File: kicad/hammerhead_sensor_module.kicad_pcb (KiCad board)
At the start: 6 copper layers, 87.5 x 58.8 mm, 138 parts, among them IC1 RT6254BHGJ6F, IC3 RT6254BHGJ6F, IC4 MAX98357AETE+T, IC6 TXB0108RGYR, J1 COMMS CONN, J10 12402012E212A, J2 APCI0105-P001A, J3 SMN-303, J4 Conn_01x22_Female, J5 Conn_01x22_Female, J6 Conn_01x03, J7 SM04B-SRSS-TBLFSN, J8 SM04B-SRSS-TBLFSN, J9 B6B-XH-A, SW1 218-2LPSTRF, U1 TPD4E05U06DQAR, U10 TPD4E05U06DQAR, U11 TPD4E05U06DQAR, U12 467651001, U13 RT9742SNGV, U14 TPD4E05U06DQAR, U15 TPD4E05U06DQAR, U16 TPD4E05U06DQAR, U17 TPD4E05U06DQAR, U18 TPD4E05U06DQAR, U19 TPD4E05U06DQAR, U2 MMBT3904TT1G, U3 TLV75733PDBVR, U4 TPD4E05U06DQAR, U5 TPD4E05U06DQAR, U6 TPD4E05U06DQAR, U7 TPD4E05U06DQAR, U8 TPD4E05U06DQAR, U9 TPD4E05U06DQAR

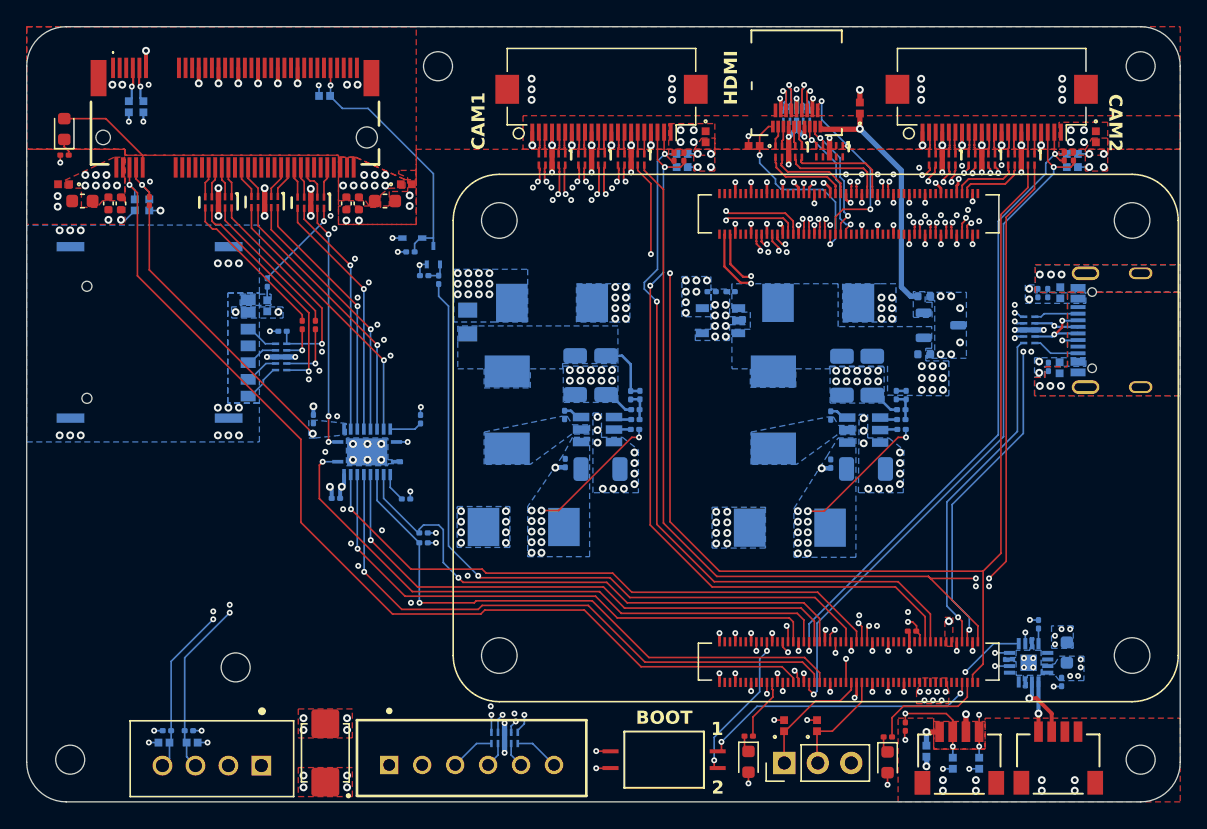
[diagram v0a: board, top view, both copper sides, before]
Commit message: update changelog v0.0.0->v0.0.1
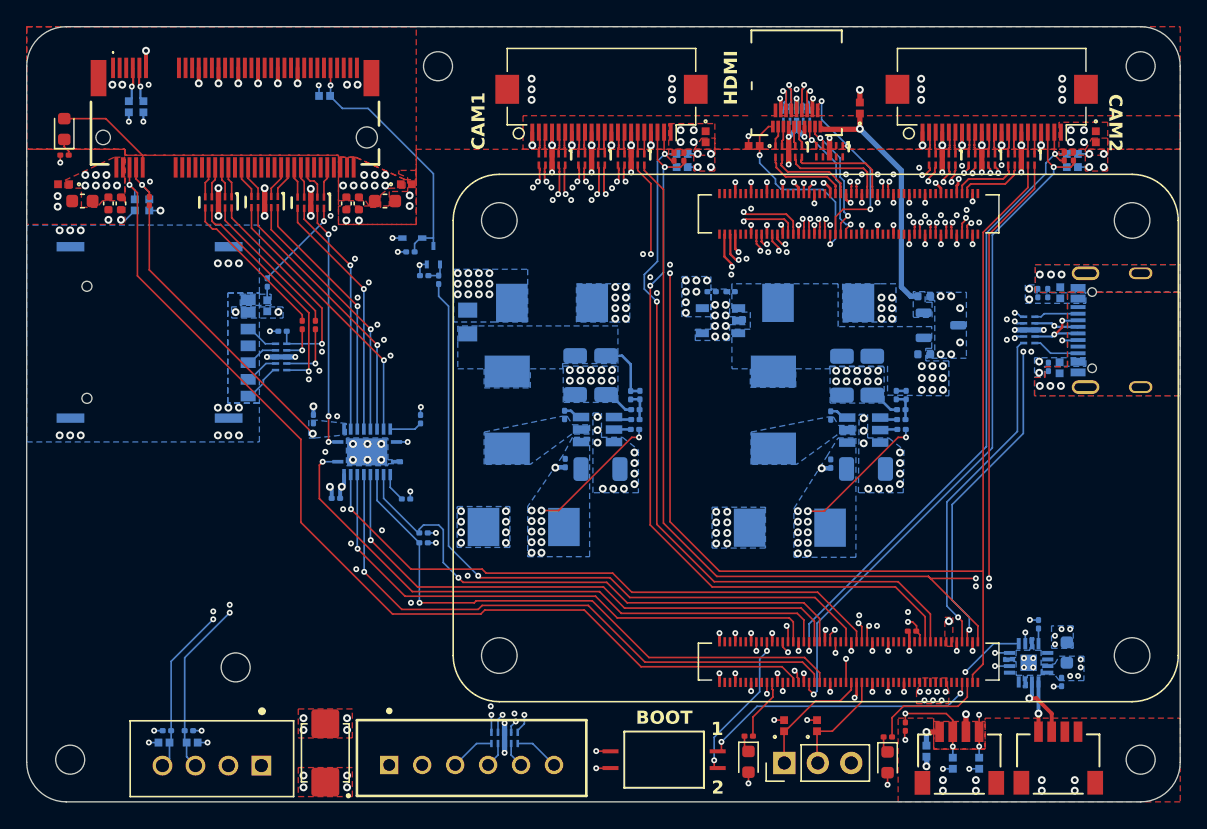
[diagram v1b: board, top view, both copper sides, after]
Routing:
- net GND: track 132.2 -> 132.7 mm, vias 347 -> 355

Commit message: add docs and cleanup
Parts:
- added R26: 2.2k 1%, Resistor_SMD:R_0201_0603Metric, B.Cu at (86.3, 52.9)
- added R30: 2.2k 1%, Resistor_SMD:R_0201_0603Metric, B.Cu at (86.3, 52.1)
- added R32: 22 <1%, Resistor_SMD:R_0201_0603Metric, B.Cu at (78.2, 54.2)
- moved R29 2.09 mm to (60.5, 35.4)
- moved D2 1.80 mm to (60.5, 37.3), turned to -90 degrees
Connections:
- D2 pad 2: /SIM7600G-H-M2B/LED1 -> 4V
- Module1 pad 91: unconnected-(Module1A-BT_nDisable-Pad91) -> GND
- R14 pad 1: 1.8V -> 3.3V
- R29 pad 1: GND -> Net-(D2-K)
- R29 pad 2: Net-(D2-K) -> /SIM7600G-H-M2B/LED1
- U17 pad 10: /SIM7600G-H-M2B/USIM_CLK -> Net-(R32-Pad1)
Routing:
- net 1.8V: track 88.6 -> 73.0 mm, vias 3 -> 4
- net 3.3V: track 20.5 -> 29.9 mm, vias 26 -> 27
- net GND: track 132.7 -> 134.6 mm, vias 355 -> 354
- net /SIM7600G-H-M2B/I2C_SDA: track 20.6 -> 22.3 mm
- net /SIM7600G-H-M2B/I2C_SCL: track 21.0 -> 22.3 mm
- net Net-(R32-Pad1): track 0.00 -> 0.85 mm
- net /SIM7600G-H-M2B/LED1: track 8.01 -> 7.46 mm

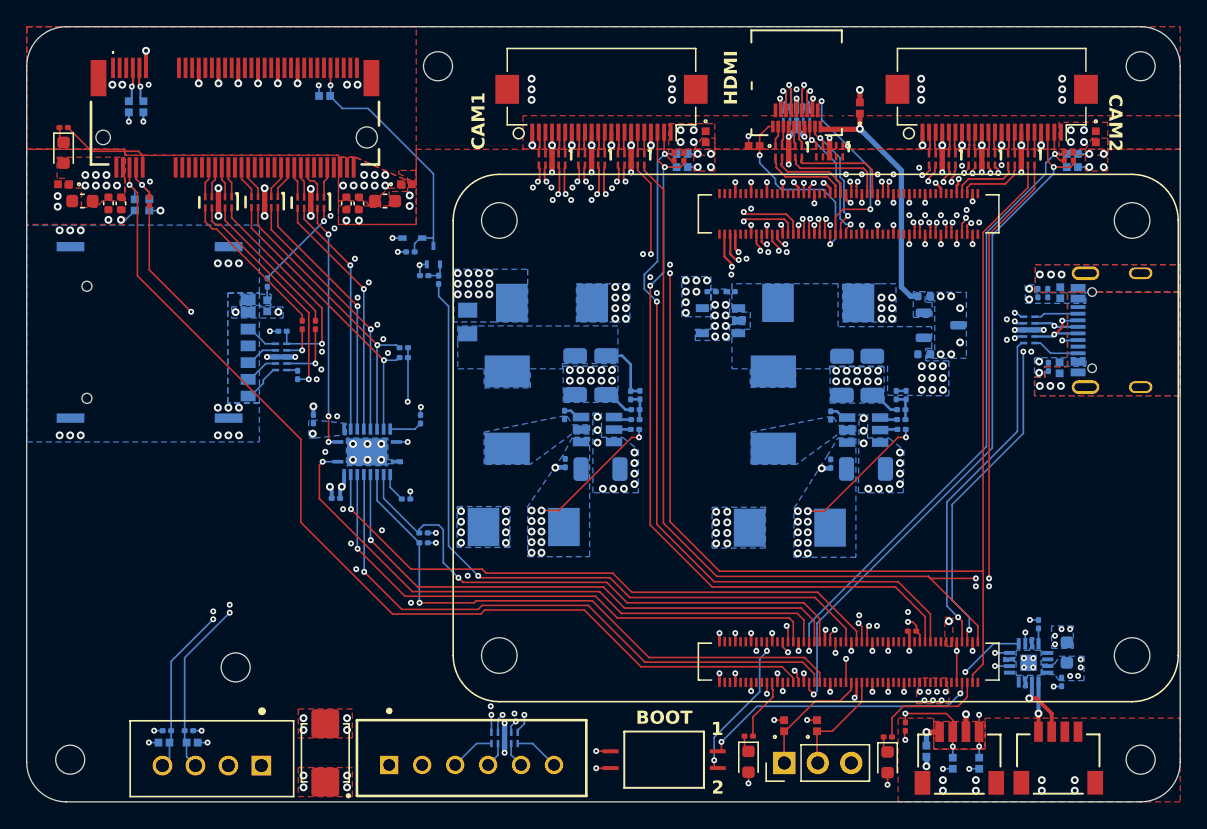
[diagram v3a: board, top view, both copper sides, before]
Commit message: assign 3d models
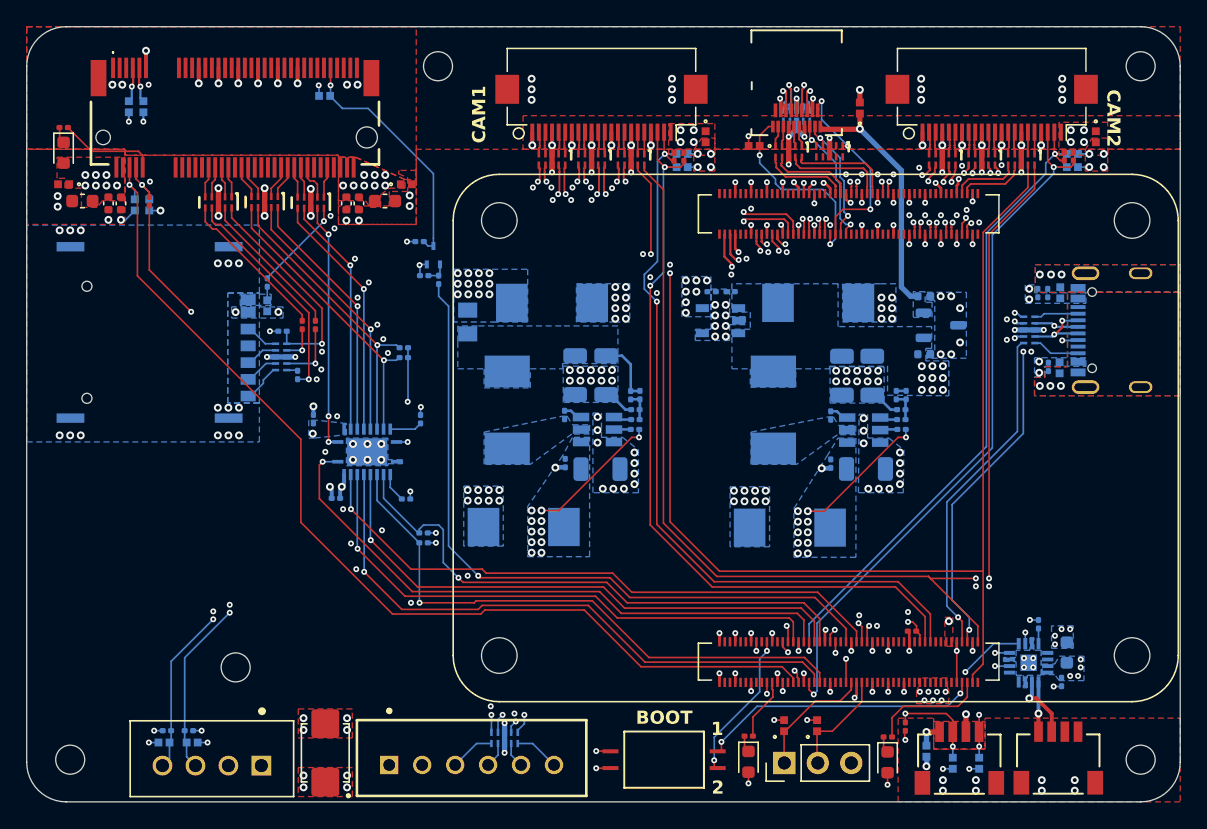
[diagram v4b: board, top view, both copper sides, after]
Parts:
- removed the D1 at (86.9, 43.8)
- moved C27 1.05 mm to (87.5, 44.0)
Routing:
- net /SIM7600G-H-M2B/RESET: track 20.1 -> 18.8 mm
- net GND: track 134.6 -> 133.8 mm, vias 354 -> 353
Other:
- board text removed: "HDMI"

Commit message: add power testpoints, add debug gpio testpoints, add comms testpoints, add logo, add component orientation silkscreen, add board name and revision silkscreen
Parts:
- added TP1: TestPoint, TestPoint:TestPoint_Pad_1.0x1.0mm, B.Cu at (134.6, 70.8)
- added TP10: TestPoint, TestPoint:TestPoint_Pad_1.0x1.0mm, B.Cu at (77.8, 36.0)
- added TP11: TestPoint, TestPoint:TestPoint_Pad_1.0x1.0mm, B.Cu at (103.0, 65.8)
- added TP12: TestPoint, TestPoint:TestPoint_Pad_1.0x1.0mm, B.Cu at (127.8, 58.8)
- added TP13: TestPoint, TestPoint:TestPoint_Pad_1.0x1.0mm, B.Cu at (70.0, 36.0)
- added TP14: TestPoint, TestPoint:TestPoint_Pad_1.0x1.0mm, B.Cu at (64.1, 79.0)
- added TP15: TestPoint, TestPoint:TestPoint_Pad_1.0x1.0mm, B.Cu at (77.9, 61.1)
- added TP16: TestPoint, TestPoint:TestPoint_Pad_1.0x1.0mm, B.Cu at (77.9, 64.3)
- added TP17: TestPoint, TestPoint:TestPoint_Pad_1.0x1.0mm, B.Cu at (106.1, 74.3)
- added TP18: TestPoint, TestPoint:TestPoint_Pad_1.0x1.0mm, B.Cu at (106.1, 77.6)
- added TP2: TestPoint, TestPoint:TestPoint_Pad_1.0x1.0mm, B.Cu at (132.2, 68.5)
- added TP3: TestPoint, TestPoint:TestPoint_Pad_1.0x1.0mm, B.Cu at (134.6, 66.0)
- added TP4: TestPoint, TestPoint:TestPoint_Pad_1.0x1.0mm, B.Cu at (132.2, 63.6)
- added TP5: TestPoint, TestPoint:TestPoint_Pad_1.0x1.0mm, B.Cu at (88.3, 60.5)
- added TP6: TestPoint, TestPoint:TestPoint_Pad_1.0x1.0mm, B.Cu at (88.3, 63.6)
- added TP7: TestPoint, TestPoint:TestPoint_Pad_1.0x1.0mm, B.Cu at (70.8, 79.0)
- added TP8: TestPoint, TestPoint:TestPoint_Pad_1.0x1.0mm, B.Cu at (67.5, 79.0)
- added TP9: TestPoint, TestPoint:TestPoint_Pad_1.0x1.0mm, B.Cu at (101.2, 33.0)
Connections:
- net /CM5_HighSpeed/USB2_N renamed /USB2_N
- net /CM5_HighSpeed/USB2_P renamed /USB2_P
- Module1 pad 45: unconnected-(Module1A-GPIO24-Pad45) -> /CM5_GPIO/TEST_GPIO_1
- Module1 pad 47: unconnected-(Module1A-GPIO23-Pad47) -> /CM5_GPIO/TEST_GPIO_2
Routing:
- net /CM5_GPIO/TEST_GPIO_1: track 0.00 -> 16.0 mm, vias 0 -> 1
- net /CM5_GPIO/TEST_GPIO_2: track 0.00 -> 15.3 mm, vias 0 -> 1
- net /CM5_GPIO/PCM_FS: track 18.2 -> 29.8 mm, vias 2 -> 3
- net /CM5_GPIO/PCM_DOUT: track 20.1 -> 31.7 mm
- net /CM5_GPIO/PCM_CLK: track 14.4 -> 21.6 mm, vias 2 -> 3
- net /SIM_I2C_SDA: track 44.5 -> 51.3 mm, vias 1 -> 3
- net /SIM_UART_RXD: track 45.6 -> 50.0 mm
- net /CM5_GPIO/SD_MODE: track 1.15 -> 4.21 mm
- net /SIM_UART_TXD: track 46.3 -> 48.7 mm
- net /CM5_GPIO/EEPROM_nWP: track 11.6 -> 14.0 mm
- net /SIM_I2C_SCL: track 42.5 -> 44.4 mm
- net /USB3-0-D_N: track 58.2 -> 59.5 mm, vias 2 -> 3
- net /PLATFORM_I2C_SCL: track 64.0 -> 65.3 mm
- net /USB3-0-D_P: track 58.1 -> 59.4 mm, vias 2 -> 3
- net /PLATFORM_I2C_SDA: track 64.6 -> 65.8 mm
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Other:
- board text added: "ACT"
- board text added: "AUDIO"
- board text added: "FAN"
- board text added: "HSM Rev A"
- board text added: "PWR"
